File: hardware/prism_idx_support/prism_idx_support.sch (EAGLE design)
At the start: 8 parts

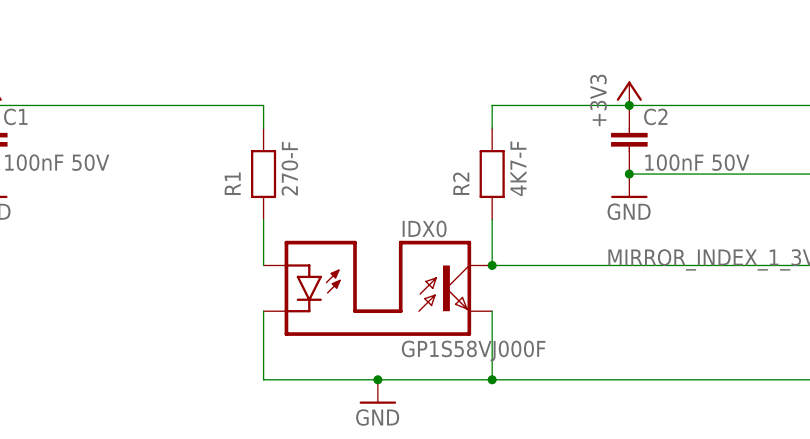
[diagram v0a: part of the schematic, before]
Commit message: resistor value modification after Damien review
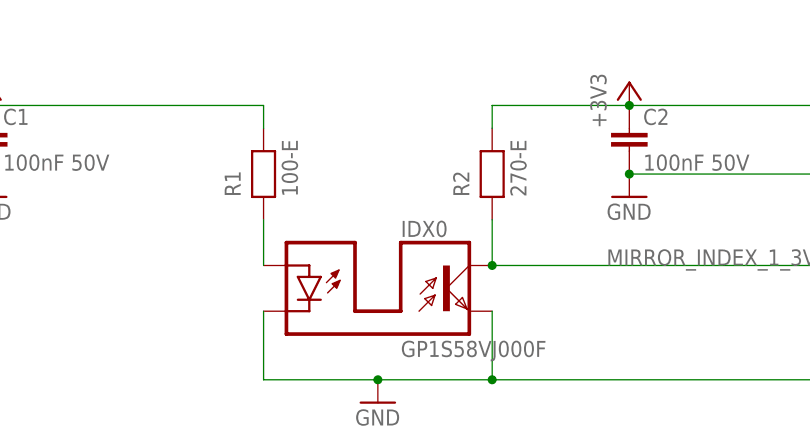
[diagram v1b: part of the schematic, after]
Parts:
- R1: value 270-F -> 100-E; device robotter_resistor:270-F -> robotter_resistor:100-E
- R2: value 4K7-F -> 270-E; device robotter_resistor:4K7-F -> robotter_resistor:270-E
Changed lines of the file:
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@@
 <part name="+3V6" library="supply1" deviceset="+3V3" device=""/>
 <part name="+3V9" library="supply1" deviceset="+3V3" device=""/>
-<part name="R2" library="robotter_resistor" deviceset="4K7" device="-F"/>
-<part name="R1" library="robotter_resistor" deviceset="270" device="-F"/>
 <part name="FRAME1" library="frames" deviceset="A4L-LOC" device=""/>
 <part name="H1" library="robotter_others" deviceset="MOUNT-PAD-ROUND" device="3.2"/>
@@
 <part name="C3" library="robotter_capacitor" deviceset="10UF" device="-C_25V" value="10µF 25V"/>
 <part name="GND1" library="supply1" deviceset="GND" device=""/>
+<part name="R2" library="robotter_resistor" deviceset="270" device="-E"/>
+<part name="R1" library="robotter_resistor" deviceset="100" device="-E" value="100-E"/>
 </parts>
 <sheets>
@@
 <instance part="+3V6" gate="G$1" x="38.1" y="91.44"/>
 <instance part="+3V9" gate="G$1" x="109.22" y="91.44"/>
-<instance part="R2" gate="G$1" x="93.98" y="81.28" rot="R90"/>
-<instance part="R1" gate="G$1" x="68.58" y="81.28" rot="R90"/>
 <instance part="FRAME1" gate="G$1" x="0" y="0"/>
 <instance part="H1" gate="G$1" x="210.82" y="63.5" rot="R90"/>
@@
 <instance part="C3" gate="G$1" x="134.62" y="86.36"/>
 <instance part="GND1" gate="1" x="210.82" y="48.26"/>
+<instance part="R2" gate="G$1" x="93.98" y="81.28" rot="R90"/>
+<instance part="R1" gate="G$1" x="68.58" y="81.28" rot="R90"/>
 </instances>
 <busses>
@@
 <pinref part="C2" gate="G$1" pin="1"/>
 <pinref part="+3V9" gate="G$1" pin="+3V3"/>
-<pinref part="R2" gate="G$1" pin="2"/>
 <wire x1="109.22" y1="88.9" x2="93.98" y2="88.9" width="0.1524" layer="91"/>
 <wire x1="93.98" y1="88.9" x2="93.98" y2="86.36" width="0.1524" layer="91"/>
@@
 <pinref part="C3" gate="G$1" pin="1"/>
 <junction x="134.62" y="88.9"/>
+<pinref part="R2" gate="G$1" pin="2"/>
 </segment>
 <segment>
@@
 <segment>
 <pinref part="IDX0" gate="G$1" pin="LED_A"/>
+<wire x1="68.58" y1="76.2" x2="68.58" y2="71.12" width="0.1524" layer="91"/>
 <pinref part="R1" gate="G$1" pin="1"/>
-<wire x1="68.58" y1="76.2" x2="68.58" y2="71.12" width="0.1524" layer="91"/>
 </segment>
 </net>
@@
 <label x="106.68" y="71.12" size="1.778" layer="95"/>
 <pinref part="IDX0" gate="G$1" pin="TRANSISTOR_C"/>
-<pinref part="R2" gate="G$1" pin="1"/>
 <wire x1="93.98" y1="76.2" x2="93.98" y2="71.12" width="0.1524" layer="91"/>
 <wire x1="93.98" y1="71.12" x2="147.32" y2="71.12" width="0.1524" layer="91"/>
 <junction x="93.98" y="71.12"/>
 <pinref part="IDX" gate="G$1" pin="IDX_3V3"/>
+<pinref part="R2" gate="G$1" pin="1"/>
 </segment>
 </net>
